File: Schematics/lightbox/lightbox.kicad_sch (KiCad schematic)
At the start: 40 parts, among them J1 Conn_01x07_Female, J2 Screw_Terminal_01x03, J3 Conn_01x12_Female, J4 Conn_01x12_Female, Q1 IRF740, SW1 SW_SP3T, SW3 SW_Push_Reset, SW4 SW_Push_+, U1 ATtiny85-20P, U2 LM317_TO-220, U3 74AHCT595, U4 74HC595, U5 D148K, U6 D148K, U7 D148K, U8 D148K

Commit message: Update Schematic and PCB layout
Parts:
- removed J3, J4: Conn_01x12_Female, Connector_PinHeader_1.27mm:PinHeader_1x12_P1.27mm_Horizontal, symbol Connector:Conn_01x12_Male
- removed U5, U6, U7, U8: D148K, Display_7Segment:D1X8K, symbol Display_Character:D148K
- added J3: Conn_01x11_Female, Connector_PinHeader_1.27mm:PinHeader_1x12_P1.27mm_Horizontal, symbol Connector:Conn_01x11_Male
- added J5: Conn_02x03_Odd_Even, Connector_PinHeader_1.27mm:PinHeader_2x03_P1.27mm_Vertical, symbol Connector_Generic:Conn_02x03_Odd_Even
- added JP1: Jumper_2_Bridged, Connector_PinHeader_1.27mm:PinHeader_1x02_P1.27mm_Vertical, symbol Jumper:Jumper_2_Bridged
- added Q1: IRF740, Package_TO_SOT_THT:TO-220-3_Vertical, symbol Transistor_FET:IRF740
- J1: renamed from J2; value Screw_Terminal_01x03 -> Screw_Terminal_01x04; footprint TerminalBlock:TerminalBlock_Altech_AK300-3_P5.00mm -> TerminalBlock:TerminalBlock_Altech_AK300-4_P5.00mm; symbol Connector:Screw_Terminal_01x03 -> Connector:Screw_Terminal_01x04
- SW2: value (none) -> SW_Push_-
- SW5: value (none) -> SW_Push_START
- renumbered D3 to D2, D4 to D3, D5 to D4, D6 to D5, D2 to D6, J1 to J2, Q1 to Q2, R3 to R1, R12 to R10, R1 to R11, R2 to R12, R4 to R2, R5 to R3, R6 to R4, R7 to R5, R8 to R6, R9 to R7, R10 to R8, R11 to R9, U3 to U2, U4 to U3, U2 to U4
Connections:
- net +3V3: now also J5.2 (Pin_2), JP1.2 (B); no longer C2.1, R11.2, U4.2 (VO)
- net A: now also J3.11 (Pin_11)
- net B: now also J3.10 (Pin_10)
- net C: now also J3.9 (Pin_9)
- net Clk: now also U1.3 (XTAL2/PB4); no longer U1.7 (PB2)
- net D: now also J3.8 (Pin_8)
- net Data: now also U1.7 (PB2), J5.3 (Pin_3); no longer U1.5 (AREF/PB0)
- net Digit1: now also J3.3 (Pin_3)
- net Digit2: now also J3.2 (Pin_2)
- net Digit3: now also J3.1 (Pin_1)
- net E: now also J3.7 (Pin_7)
- net F: now also J3.6 (Pin_6)
- net G: now also J3.5 (Pin_5)
- net GND: now also J1.4 (Pin_4), J5.6 (Pin_6), Q1.3 (S); no longer D1.1 (K), D6.1 (K), J1.3 (Pin_3)
- net H: now also J3.4 (Pin_4)
- net Keypad: now also U1.5 (AREF/PB0), J5.4 (Pin_4); no longer U1.2 (XTAL1/PB3)
- net Rclk: now also U1.2 (XTAL1/PB3); no longer U1.6 (PB1)
- net ISP_RST: now reaches U1.1 (~{RESET}/PB5)
- net ISP_RST: now also J5.5 (Pin_5)
- net Digit4 renamed REDLeds
- net REDLeds: now also Q1.1 (G)
- net Led_Array renamed UV_Led_Array
- net Leds renamed UVLeds
- net UVLeds: now also U1.6 (PB1), J5.1 (Pin_1); no longer U1.3 (XTAL2/PB4)
- new net: C2.1, JP1.1 (A), R11.2, U4.2 (VO)
- new net RED_Led_Array: D1.1 (K), D6.1 (K), J1.3 (Pin_3), Q1.2 (D)
- no-connect marks 2 -> 1
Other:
- added sheet 8SegmentDisplay (8SegmentDisplay/8SegmentDisplay.kicad_sch)
- moved on the sheet: C1, C2, D1, D2, D3, D4, D5, D6, D7, D8, J2, Q2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

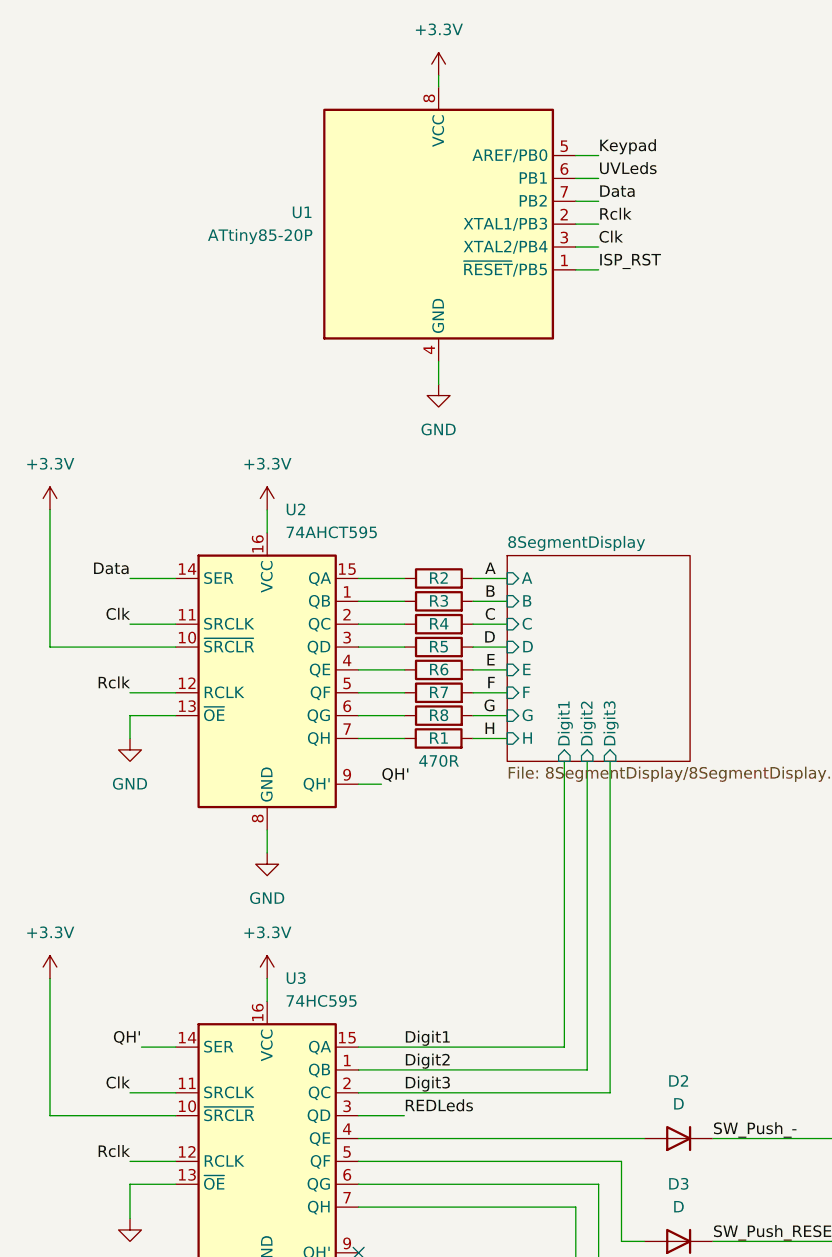
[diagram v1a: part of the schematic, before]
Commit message: Update schematics for new buzzer
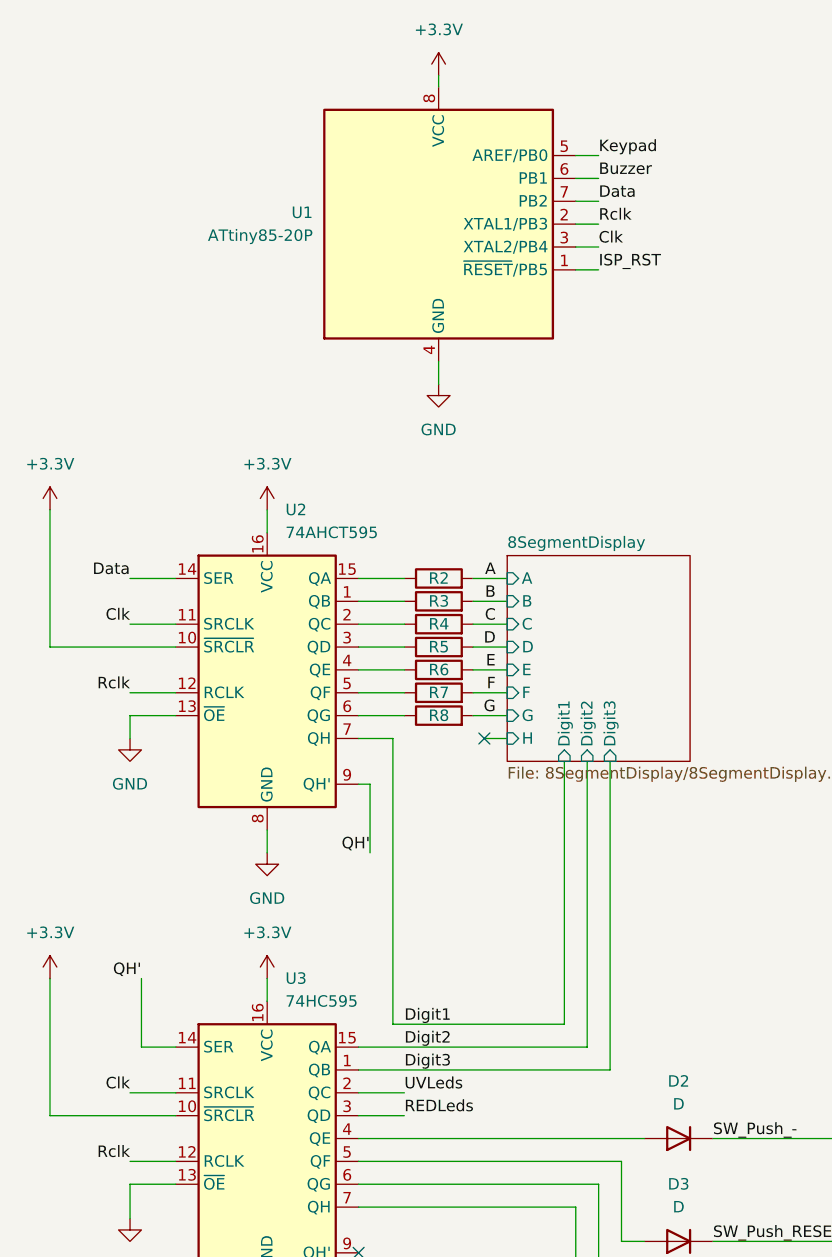
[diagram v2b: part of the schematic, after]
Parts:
- removed R1: 470R, Resistor_THT:R_Axial_DIN0204_L3.6mm_D1.6mm_P5.08mm_Vertical, symbol Device:R
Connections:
- net Digit1: now also U2.7 (QH); no longer U3.15 (QA)
- net Digit2: now also U3.15 (QA); no longer U3.1 (QB)
- net Digit3: now also U3.1 (QB); no longer U3.2 (QC)
- net UVLeds: now also U3.2 (QC); no longer U1.6 (PB1)
- new net Buzzer: U1.6 (PB1)
- no-connect marks 1 -> 2
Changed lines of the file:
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@@
   (junction (at 182.88 129.54) (diameter 0) (color 0 0 0 0)
   )
+  (no_connect (at 82.55 102.87))
   (no_connect (at 68.58 160.02))
+  (wire (pts (xy 44.45 137.16) (xy 48.26 137.16))
+    (stroke (width 0) (type default) (color 0 0 0 0))
+  )
   (wire (pts (xy 180.34 83.82) (xy 180.34 86.36))
     (stroke (width 0) (type default) (color 0 0 0 0))
@@
     (stroke (width 0) (type default) (color 0 0 0 0))
   )
+  (wire (pts (xy 91.44 134.62) (xy 72.39 134.62))
+    (stroke (width 0) (type default) (color 0 0 0 0))
+  )
   (wire (pts (xy 182.88 120.65) (xy 190.5 120.65))
     (stroke (width 0) (type default) (color 0 0 0 0))
@@
     (stroke (width 0) (type default) (color 0 0 0 0))
   )
-  (wire (pts (xy 68.58 102.87) (xy 73.66 102.87))
-    (stroke (width 0) (type default) (color 0 0 0 0))
-  )
   (wire (pts (xy 43.18 97.79) (xy 48.26 97.79))
     (stroke (width 0) (type default) (color 0 0 0 0))
@@
     (stroke (width 0) (type default) (color 0 0 0 0))
   )
-  (wire (pts (xy 81.28 102.87) (xy 85.09 102.87))
-    (stroke (width 0) (type default) (color 0 0 0 0))
-  )
   (wire (pts (xy 161.29 138.43) (xy 156.21 138.43))
     (stroke (width 0) (type default) (color 0 0 0 0))
@@
     (stroke (width 0) (type default) (color 0 0 0 0))
   )
-  (wire (pts (xy 96.52 105.41) (xy 96.52 142.24))
+  (wire (pts (xy 96.52 105.41) (xy 96.52 139.7))
     (stroke (width 0) (type default) (color 0 0 0 0))
   )
@@
     (stroke (width 0) (type default) (color 0 0 0 0))
   )
+  (wire (pts (xy 91.44 105.41) (xy 91.44 134.62))
+    (stroke (width 0) (type default) (color 0 0 0 0))
+  )
   (wire (pts (xy 68.58 100.33) (xy 73.6896 100.33))
     (stroke (width 0) (type default) (color 0 0 0 0))
   )
+  (wire (pts (xy 68.58 142.24) (xy 73.66 142.24))
+    (stroke (width 0) (type default) (color 0 0 0 0))
+  )
   (wire (pts (xy 147.32 41.91) (xy 147.32 45.72))
     (stroke (width 0) (type default) (color 0 0 0 0))
@@
     (stroke (width 0) (type default) (color 0 0 0 0))
   )
+  (wire (pts (xy 72.39 102.87) (xy 72.39 134.62))
+    (stroke (width 0) (type default) (color 0 0 0 0))
+  )
   (wire (pts (xy 97.79 149.86) (xy 97.79 158.75))
     (stroke (width 0) (type default) (color 0 0 0 0))
@@
     (stroke (width 0) (type default) (color 0 0 0 0))
   )
-  (wire (pts (xy 68.58 142.24) (xy 96.52 142.24))
-    (stroke (width 0) (type default) (color 0 0 0 0))
-  )
   (wire (pts (xy 180.34 74.93) (xy 185.42 74.93))
     (stroke (width 0) (type default) (color 0 0 0 0))
@@
     (stroke (width 0) (type default) (color 0 0 0 0))
   )
+  (wire (pts (xy 69.85 107.95) (xy 68.58 107.95))
+    (stroke (width 0) (type default) (color 0 0 0 0))
+  )
   (wire (pts (xy 161.29 120.65) (xy 161.29 125.73))
     (stroke (width 0) (type default) (color 0 0 0 0))
@@
     (stroke (width 0) (type default) (color 0 0 0 0))
   )
+  (wire (pts (xy 68.58 137.16) (xy 93.98 137.16))
+    (stroke (width 0) (type default) (color 0 0 0 0))
+  )
   (wire (pts (xy 190.5 133.35) (xy 190.5 138.43))
     (stroke (width 0) (type default) (color 0 0 0 0))
@@
     (stroke (width 0) (type default) (color 0 0 0 0))
   )
-  (wire (pts (xy 68.58 137.16) (xy 91.44 137.16))
-    (stroke (width 0) (type default) (color 0 0 0 0))
-  )
   (wire (pts (xy 238.76 63.5) (xy 243.84 63.5))
     (stroke (width 0) (type default) (color 0 0 0 0))
@@
     (stroke (width 0) (type default) (color 0 0 0 0))
   )
-  (wire (pts (xy 68.58 139.7) (xy 93.98 139.7))
-    (stroke (width 0) (type default) (color 0 0 0 0))
-  )
   (wire (pts (xy 134.62 184.15) (xy 139.7 184.15))
     (stroke (width 0) (type default) (color 0 0 0 0))
@@
     (stroke (width 0) (type default) (color 0 0 0 0))
   )
+  (wire (pts (xy 82.55 102.87) (xy 85.09 102.87))
+    (stroke (width 0) (type default) (color 0 0 0 0))
+  )
+  (wire (pts (xy 68.58 139.7) (xy 96.52 139.7))
+    (stroke (width 0) (type default) (color 0 0 0 0))
+  )
   (wire (pts (xy 144.78 66.04) (xy 144.78 69.85))
     (stroke (width 0) (type default) (color 0 0 0 0))
@@
     (stroke (width 0) (type default) (color 0 0 0 0))
   )
-  (wire (pts (xy 44.45 137.16) (xy 48.26 137.16))
+  (wire (pts (xy 68.58 102.87) (xy 72.39 102.87))
+    (stroke (width 0) (type default) (color 0 0 0 0))
+  )
+  (wire (pts (xy 44.45 129.54) (xy 44.45 137.16))
     (stroke (width 0) (type default) (color 0 0 0 0))
   )
@@
     (stroke (width 0) (type default) (color 0 0 0 0))
   )
-  (wire (pts (xy 91.44 105.41) (xy 91.44 137.16))
-    (stroke (width 0) (type default) (color 0 0 0 0))
-  )
   (wire (pts (xy 245.11 40.64) (xy 247.65 40.64))
     (stroke (width 0) (type default) (color 0 0 0 0))
   )
-  (wire (pts (xy 93.98 105.41) (xy 93.98 139.7))
+  (wire (pts (xy 93.98 105.41) (xy 93.98 137.16))
     (stroke (width 0) (type default) (color 0 0 0 0))
   )
@@
     (stroke (width 0) (type default) (color 0 0 0 0))
   )
-  (wire (pts (xy 68.58 107.95) (xy 71.12 107.95))
+  (wire (pts (xy 69.85 107.95) (xy 69.85 115.57))
     (stroke (width 0) (type default) (color 0 0 0 0))
   )
@@
     (effects (font (size 1.27 1.27)) (justify right bottom))
   )
+  (label "Buzzer" (at 95.25 40.64 0)
+    (effects (font (size 1.27 1.27)) (justify left bottom))
+  )
   (label "Keypad" (at 243.84 105.41 180)
     (effects (font (size 1.27 1.27)) (justify right bottom))
@@
     (effects (font (size 1.27 1.27)) (justify left bottom))
   )
+  (label "UVLeds" (at 73.66 142.24 0)
+    (effects (font (size 1.27 1.27)) (justify left bottom))
+  )
   (label "UV_Led_Array" (at 238.76 120.65 180)
     (effects (font (size 1.27 1.27)) (justify right bottom))
@@
     (effects (font (size 1.27 1.27)) (justify right bottom))
   )
-  (label "Digit3" (at 73.66 142.24 0)
+  (label "Digit3" (at 73.66 139.7 0)
     (effects (font (size 1.27 1.27)) (justify left bottom))
   )
@@
     (effects (font (size 1.27 1.27)) (justify right bottom))
   )
-  (label "H" (at 83.82 102.87 180)
-    (effects (font (size 1.27 1.27)) (justify right bottom))
-  )
-  (label "UVLeds" (at 95.25 40.64 0)
-    (effects (font (size 1.27 1.27)) (justify left bottom))
-  )
   (label "ISP_RST" (at 245.11 40.64 180)
     (effects (font (size 1.27 1.27)) (justify right bottom))
@@
     (effects (font (size 1.27 1.27)) (justify right bottom))
   )
-  (label "QH'" (at 71.12 107.95 0)
-    (effects (font (size 1.27 1.27)) (justify left bottom))
+  (label "QH'" (at 69.85 115.57 180)
+    (effects (font (size 1.27 1.27)) (justify right bottom))
   )
   (label "Keypad" (at 262.89 38.1 0)
@@
     (effects (font (size 1.27 1.27)) (justify left bottom))
   )
-  (label "Digit2" (at 73.66 139.7 0)
+  (label "Digit2" (at 73.66 137.16 0)
     (effects (font (size 1.27 1.27)) (justify left bottom))
   )
@@
     (effects (font (size 1.27 1.27)) (justify right bottom))
   )
+  (label "Digit1" (at 73.66 134.62 0)
+    (effects (font (size 1.27 1.27)) (justify left bottom))
+  )
   (label "Keypad" (at 152.4 165.1 0)
     (effects (font (size 1.27 1.27)) (justify left bottom))
@@
     (effects (font (size 1.27 1.27)) (justify right bottom))
   )
-  (label "Digit1" (at 73.66 137.16 0)
-    (effects (font (size 1.27 1.27)) (justify left bottom))
-  )
   (label "C" (at 238.76 78.74 180)
     (effects (font (size 1.27 1.27)) (justify right bottom))
   )
-  (label "QH'" (at 44.45 137.16 180)
+  (label "QH'" (at 44.45 129.54 180)
     (effects (font (size 1.27 1.27)) (justify right bottom))
   )
@@
     )
     (property "Datasheet" "~" (id 3) (at 77.4996 97.79 0)
-      (effects (font (size 1.27 1.27)) hide)
-    )
-    (pin "1")
-    (pin "2")
-  )
-  (symbol (lib_id "Device:R") (at 77.47 102.87 90) (unit 1)
-    (in_bom yes) (on_board yes)
-    (property "Reference" "R1" (id 0) (at 77.4996 102.87 90))
-    (property "Value" "470R" (id 1) (at 77.4996 105.41 90))
-    (property "Footprint" "Resistor_THT:R_Axial_DIN0204_L3.6mm_D1.6mm_P5.08mm_Vertical" (id 2) (at 77.47 104.648 90)
-      (effects (font (size 1.27 1.27)) hide)
-    )
-    (property "Datasheet" "~" (id 3) (at 77.47 102.87 0)
       (effects (font (size 1.27 1.27)) hide)
     )
@@
       (reference "Q2") (unit 1) (value "IRF740") (footprint "Package_TO_SOT_THT:TO-220-3_Vertical")
     )
-    (path "/273d802d-0a8a-48a2-a856-f7d05eba969a"
-      (reference "R1") (unit 1) (value "470R") (footprint "Resistor_THT:R_Axial_DIN0204_L3.6mm_D1.6mm_P5.08mm_Vertical")
-    )
     (path "/524d1d1c-f720-4dd7-b8c7-be1393e3f5f7"

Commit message: remove unnecessary diodes
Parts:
- removed D2, D3, D4, D5: D, Diode_THT:D_A-405_P7.62mm_Horizontal, symbol Device:D
- added BZ1: Buzzer, Buzzer_Beeper:MagneticBuzzer_ProSignal_ABI-010-RC, symbol Device:Buzzer
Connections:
- net Buzzer: now also J5.1 (Pin_1), U1.5 (AREF/PB0), BZ1.1 (-); no longer U1.6 (PB1)
- net GND: now also BZ1.2 (+)
- net Keypad: now also U1.6 (PB1); no longer U1.5 (AREF/PB0)
- net SW_Push_+: now also U3.6 (QG)
- net SW_Push_-: now also U3.4 (QE)
- net SW_Push_RESET: now also U3.5 (QF)
- net SW_Push_START: now also U3.7 (QH)
- net UVLeds: no longer J5.1 (Pin_1)
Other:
- moved on the sheet: R9, SW2, SW3, SW4, SW5

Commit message: Fix annotations
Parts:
- renumbered D6 to D2, D7 to D3, D8 to D4, J3 to J2, J2 to J3, J5 to J4, R2 to R1, R11 to R10, R12 to R11, R3 to R2, R4 to R3, R5 to R4, R6 to R5, R7 to R6, R8 to R7, R9 to R8, R10 to R9, SW2 to SW1, SW3 to SW2, SW4 to SW3, SW5 to SW4, SW1 to SW5, U2 to U1, U3 to U2, U1 to U3

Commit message: Update schematics
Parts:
- added Q?: IRF740, Package_TO_SOT_THT:TO-220-3_Vertical, symbol Transistor_FET:IRF740
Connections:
- net +12V: now also Q?.2 (D)
- net Buzzer: now also J4.4 (Pin_4), Q?.1 (G); no longer BZ1.1 (-), J4.1 (Pin_1)
- net Data renamed D_{2}
- net Keypad renamed D_{1}
- net D_{1}: now also J4.1 (Pin_1); no longer J4.4 (Pin_4)
- net Rclk renamed D_{3}
- new net: BZ1.1 (-), Q?.3 (S)
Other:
- moved on the sheet: BZ1
